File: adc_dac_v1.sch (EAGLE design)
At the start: 24 parts, among them IC2 LT6220, IC4 LT6220, U2 DAC8832IRGYR, U4 OPA353NA/3K, U7 DAC8832IRGYR, U8 OPA353NA/3K

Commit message: updates to DAC design
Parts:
- removed C16, C18: DNP, rcl:C-USC0603
- removed C17, C19, C20: 0.1u, rcl:C-USC0603
- removed IC4: LT6220, linear:MCP601SN
- removed R13, R14, R15, R16, R6, R8: 0, rcl:R-US_R0603
- removed U4, U8: OPA353NA/3K, AD7960:OPA353NA/3K
- removed U7: DAC8832IRGYR, AD7960:DAC8832IRGYR
- added C1, C2: 0.1u, rcl:C-USC0603
- added C3: 2p, rcl:C-USC0603
- added IC1: LT6220, linear:MCP601SN
- added R1: 10k, rcl:R-US_R0603
- added R2, R3: 60k, rcl:R-US_R0603
- added R4: 0, rcl:R-US_R0603
- added U1: OPA353NA/3K, open_covg:OPA353NA/3K
- U2: value DAC8832IRGYR -> AD5453YRMZ-REEL7; device AD7960:DAC8832IRGYR -> open_covg:AD5453YRMZ-REEL7
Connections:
- removed net N$15: R14.1, U7.RFB
- removed net N$16: R16.1, U7.!LDAC
- removed net N$8: R8.1, U2.!LDAC
- new net CLK+: R2.1, U1.CLK+
- new net CLK-: R2.2, U1.CLK-
- new net CNV+: U1.CNV+
- new net CNV-: U1.CNV-
- new net D+: U1.D+
- new net D-: U1.D-
- new net DCO+: U1.DCO+
- new net DCO-: U1.DCO-
- new net DIFF_IN+: R4.1
- new net EN0: U1.EN0
- new net EN1: U1.EN1
- new net EN2: U1.EN2
- new net EN3: U1.EN3
- new net IN-: U1.IN-
- new net N$1: C3.1, IC1.+IN, IC1.IN-, IC1.OUT, R1.1, U2.IOUT1
- new net N$4: IC1.OUT, R1.1, R4.2, U1.VDD2_3
- new net REF_5V: IC1.IN+
- net +5V: now also C1.1, IC1.V+, U1.VDD1, U1.VDD1_2, U1.VDD1_3; no longer C19.1, IC4.V+
- net -5V: now also C2.1, IC1.V-; no longer C20.1, IC4.V-
- net 1.8V: now also C3.1, U1.VDD2, U1.VDD2_2, U1.VIO
- net 3V3: now also C2.1, U1.V+, U1.VDD; no longer C17.1, U4.V+, U7.VDD, U8.V+
- net 3V3_REF: now also U1.IN+; no longer U4.IN+, U8.IN+
- net AGND: now also C1.2, C2.2, C3.2, IC1.-IN, IC2.-IN, R4.1, R4.2, U1.!LDAC, U1.AGNDF, U1.AGNDS, U1.DGND, U1.EPAD, U1.V-, U2.GND; no longer C16.2, C17.2, C18.2, C19.2, C20.2, R16.2, R8.2, U2.AGNDF, U2.AGNDS, U2.DGND, U2.EPAD, U4.V-, U7.AGNDF, U7.AGNDS, U7.DGND, U7.EPAD, U8.V-
- net AMP_PWR+: now also C1.1, IC1.+VS
- net CSB: now also U1.!CS, U2.SYNCB; no longer U2.!CS, U7.!CS
- net DAC_VAL: now also IC1.+IN, U1.VOUT; no longer IC2.+IN, IC4.+IN, U2.VOUT, U7.VOUT
- net GND: now also C1.2, C2.2, C3.2, IC1.-VS, R3.1, U1.EPAD, U1.GND, U1.GND_2, U1.REFIN, U1.REF_GND, U1.REF_GND_2, U1.REF_GND_3
- net IN+: now also U1.IN+; no longer R13.2
- net N$11: no longer R6.1, R8.2
- net N$12: no longer R6.2
- net N$13: no longer IC4.-IN, IC4.OUT, R14.2, R15.1, U7.INV
- net N$14: no longer R13.1, U8.OUT
- net N$2: now also C3.2, IC1.-IN, IC1.OUT, R2.2, R3.1, R4.1, R4.2, U1.INV, U2.RFB; no longer R8.1
- net N$3: now also C2.1, IC2.+IN, R1.2, R2.1, R3.2, U1.RFB
- net N$5: now also R2.2; no longer IC2.-IN, R13.1, R6.2, U2.INV
- net N$6: now also C1.1, R1.2, U1.OUT, U1.VREF-F, U1.VREF-S; no longer U4.OUT
- net N$7: now also R3.1, U2.VREF; no longer R6.1, U2.RFB
- net OUT: now also C3.1, R3.2; no longer C18.1, R15.2
- net REF: now also R1.2, U1.REF, U1.REF_2, U1.REF_3, U1.REF_4
- net SCLK: now also U1.SCLK; no longer U7.SCLK
- net SDI: now also U1.SDI, U2.SDIN; no longer U2.SDI, U7.SDI
- net VCM: now also U1.VCM
- net VREF_BUF: now also U1.IN-; no longer C16.1, R13.2, U2.VREF-F, U2.VREF-S, U4.IN-, U7.VREF-F, U7.VREF-S, U8.IN-
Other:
- note added: "VDD should match level of SPI interface VREF VR02"
- moved on the sheet: C10, C6, C7, C8, C9, IC2, R5, R7

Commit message: updates to README and tracker
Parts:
- removed U1: OPA353NA/3K, open_covg:OPA353NA/3K
- added IC3: ADA4001-2, analog-devices:ADA4692-2R
- added R6: 0, rcl:R-US_R0603
- IC2: value LT6220 -> OPA353NA3K
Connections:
- removed net CNV+: U1.CNV+
- removed net CNV-: U1.CNV-
- removed net D+: U1.D+
- removed net D-: U1.D-
- removed net DCO+: U1.DCO+
- removed net DCO-: U1.DCO-
- removed net EN0: U1.EN0
- removed net EN1: U1.EN1
- removed net EN2: U1.EN2
- removed net EN3: U1.EN3
- removed net IN+: U1.IN+
- removed net IN-: U1.IN-
- new net +15V: C9.1, IC3P.V+
- new net -15V: C10.1, IC3P.V-
- new net N$8: IC2.V+
- net +5V: no longer IC2.V+, U1.VDD1, U1.VDD1_2, U1.VDD1_3
- net -5V: no longer C10.1, IC2.V-
- net 1.8V: no longer U1.VDD2, U1.VDD2_2, U1.VIO
- net 3V3: no longer U1.V+, U1.VDD
- net 3V3_REF: now also IC2.+IN; no longer U1.IN+
- net AGND: now also IC2.V-, IC3A.IN-; no longer IC2.-IN, U1.!LDAC, U1.AGNDF, U1.AGNDS, U1.DGND, U1.EPAD, U1.V-
- net CLK+: no longer U1.CLK+
- net CLK-: no longer U1.CLK-
- net CSB: no longer U1.!CS
- net DAC_VAL: no longer U1.VOUT
- net GND: no longer U1.EPAD, U1.GND, U1.GND_2, U1.REFIN, U1.REF_GND, U1.REF_GND_2, U1.REF_GND_3
- net N$11: now also R6.1
- net N$12: now also R6.2
- net N$2: no longer U1.INV
- net N$3: now also IC3A.IN+; no longer IC2.+IN, U1.RFB
- net N$4: no longer U1.VDD2_3
- net N$5: now also IC3A.OUT; no longer IC2.OUT
- net N$6: now also IC2.OUT; no longer U1.OUT, U1.VREF-F, U1.VREF-S
- net REF: no longer U1.REF, U1.REF_2, U1.REF_3, U1.REF_4
- net SCLK: no longer U1.SCLK
- net SDI: no longer U1.SDI
- net VCM: no longer U1.VCM
- net VREF_BUF: now also IC2.-IN; no longer U1.IN-
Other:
- moved on the sheet: C6, C9, IC2, R5

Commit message: ulp cleanup
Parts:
- added BRD1: OPALKELLY_XEM6310, open_covg:OPALKELLY_XEM6310
- added C11, C12, C14, C15, C16, C17, C18: 0.1u, rcl:C-USC0805
- added C13, C5: 10u, rcl:C-USC0805
- added C19, C20: DNP, rcl:C-USC0805
- added C4: 100p, rcl:C-USC0805
- added IC4: AD8031RJ, analog-devices:AD8031RJ
- added R10, R11, R8, R9: 499, rcl:R-US_R0603
- added R12, R13: 100, rcl:R-US_R0603
- added R14, R16, R17: 0, rcl:R-US_R0603
- added R15: DNP, rcl:R-US_R0603
- added R18: DNO, rcl:R-US_R0603
- added R19, R20: 33, rcl:R-US_R0603
- added U1: AD7960BCPZ-RL7, AD7960:AD7960BCPZ-RL7
- added U3: ADA4932-1YCPZ-R7, AD7960:ADA4932-1YCPZ-R7
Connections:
- new net CNV+: R10.2, R12.2, U1.CNV+
- new net CNV-: R10.1, R12.1, U1.CNV-
- new net D+: U1.D+
- new net D-: U1.D-
- new net DCO+: U1.DCO+
- new net DCO-: U1.DCO-
- new net DGND: BRD1JP2_ODD.DGND_1
- new net EN0: U1.EN0
- new net EN1: U1.EN1
- new net EN2: U1.EN2
- new net EN3: U1.EN3
- new net IN+: C4.2, R13.2, R20.2, U1.IN+
- new net IN-: C4.1, R12.2, R19.2, U1.IN-
- new net N$10: IC4.IN-, IC4.OUT, R14.1
- new net N$15: C20.1, R10.1, R16.2, R18.1
- new net N$16: C19.1, R11.1, R15.2, R17.2
- new net N$17: R19.1, U3.OUT-
- new net N$18: R20.1, U3.OUT+
- new net N$19: BRD1JP2_ODD.JTAG_TCK
- new net N$20: BRD1JP2_ODD.JTAG_TMS
- new net N$21: BRD1JP2_ODD.JTAG_TDI
- new net N$22: BRD1JP2_ODD.G16-L9P_1
- new net N$9: U1.VDD2_3
- new net TEST_NET_NAME: BRD1JP2_EVEN.+3.3VDD_2
- net +5V: now also C11.1, C14.1, C15.1, C17.1, C4.1, U1.VDD1, U1.VDD1_2, U1.VDD1_3
- net -5V: now also C5.1
- net 1.8V: now also C11.1, C16.1, U1.VDD2, U1.VDD2_2, U1.VIO
- net 3V3: now also U1.VDD, U3.V+
- net 3V3_REF: now also U3.IN+
- net AGND: now also C4.2, C5.2, U1.!LDAC, U1.AGNDF, U1.AGNDS, U1.DGND, U1.EPAD, U3.V-
- net AMP_PWR+: now also C18.1, IC4.+VS, U3.PD, U3.VS+, U3.VS+_2, U3.VS+_3, U3.VS+_4
- net AMP_PWR-: now also U3.VS-, U3.VS-_2, U3.VS-_3, U3.VS-_4
- net CLK+: now also R13.1, U1.CLK+
- net CLK-: now also R13.2, U1.CLK-
- net CSB: now also U1.!CS
- net DAC_VAL: now also U1.VOUT
- net DIFF_IN+: now also R16.1
- net DIFF_IN-: now also R17.1
- net GND: now also C11.2, C12.2, C13.2, C14.2, C15.2, C16.2, C17.2, C18.2, C19.2, C20.2, C5.2, IC4.-VS, R11.2, R15.1, R18.2, U1.EPAD, U1.GND, U1.GND_2, U1.REFIN, U1.REF_GND, U1.REF_GND_2, U1.REF_GND_3, U3.EPAD
- net N$11: now also R10.2, R8.1, R8.2, U3.IN+
- net N$12: now also R8.2, U3.FB-
- net N$13: now also R11.2, R9.1, R9.2, U3.IN-
- net N$14: now also R9.2, U3.FB+
- net N$2: now also C12.1, R11.1, R8.1, U1.INV
- net N$3: now also R9.1, U1.RFB
- net N$4: now also U1.VDD2_3, U3.OUT
- net N$5: now also R13.1
- net N$6: now also R12.1, U1.VREF-F, U1.VREF-S, U3.IN-
- net REF: now also C12.1, C13.1, R14.2, U1.REF, U1.REF_2, U1.REF_3, U1.REF_4
- net REF_5V: now also IC4.IN+
- net SCLK: now also U1.SCLK
- net SDI: now also U1.SDI
- net VCM: now also C5.1, U1.VCM, U3.VOCM

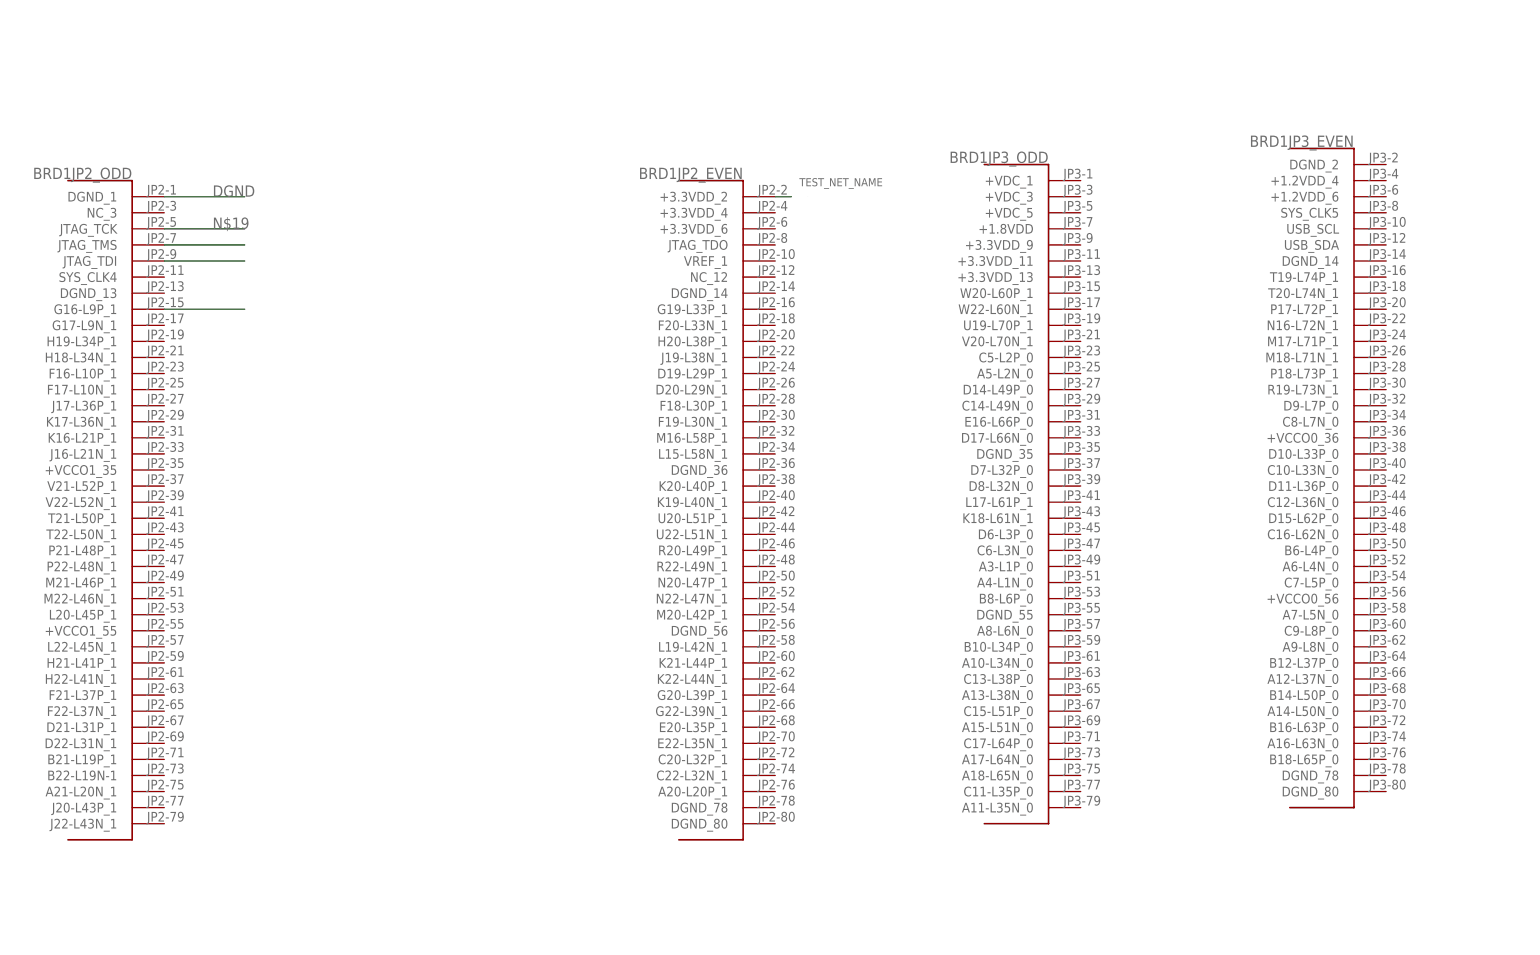
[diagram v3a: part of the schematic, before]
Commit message: updates to ULP and helper python to create script that labels samtech
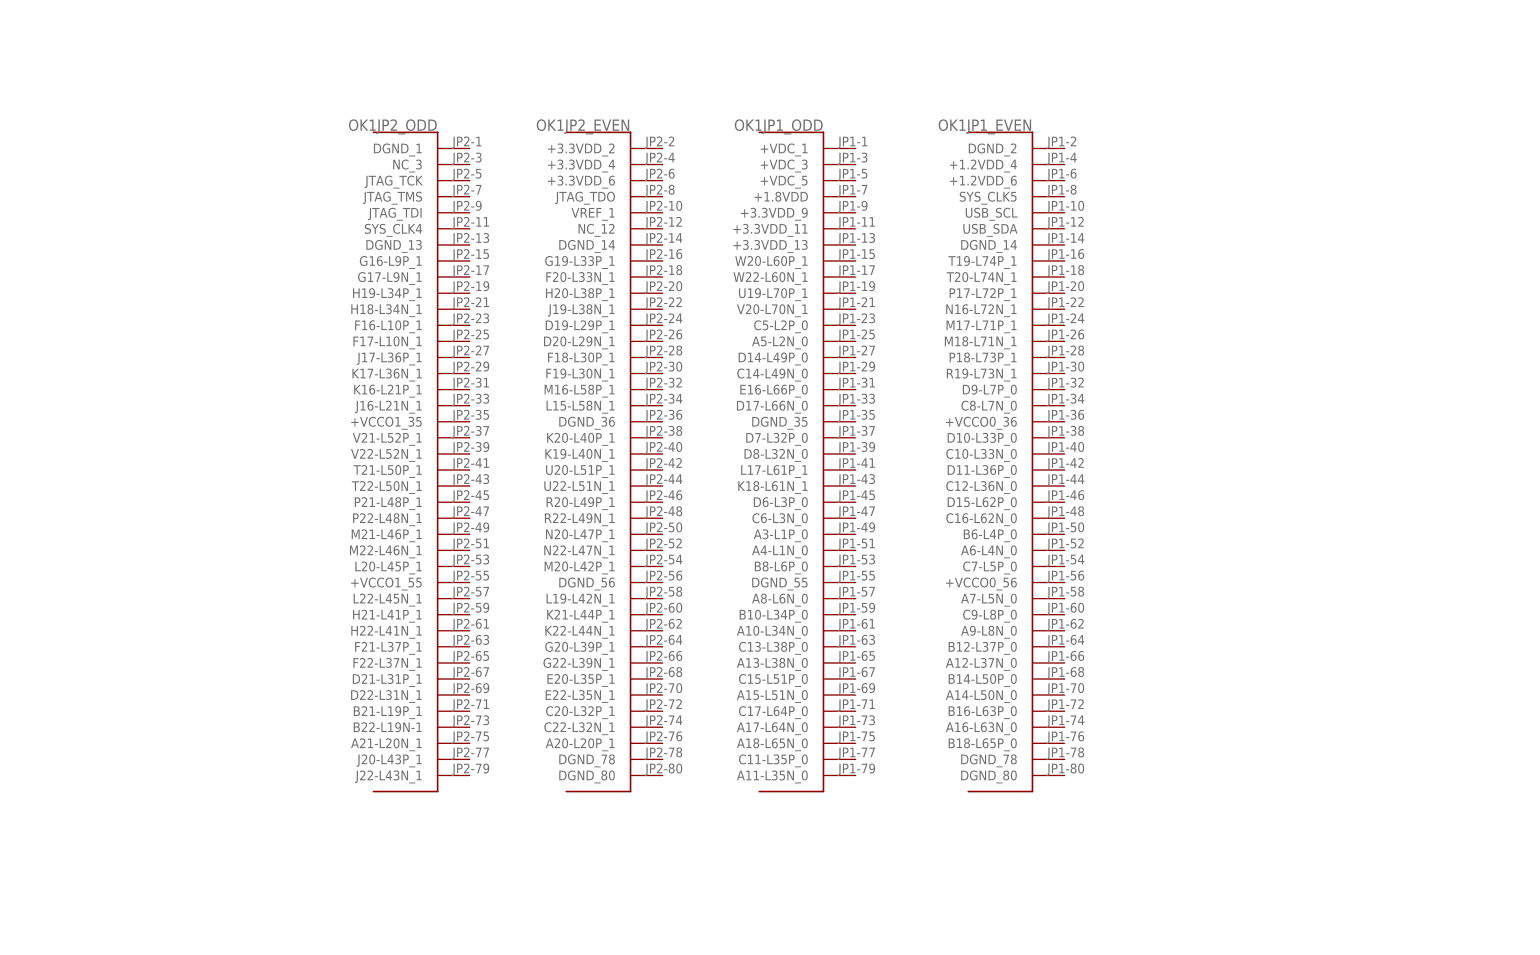
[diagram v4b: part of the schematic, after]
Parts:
- removed BRD1: OPALKELLY_XEM6310, open_covg:OPALKELLY_XEM6310
- added OK1: OPALKELLY_XEM6310, open_covg:OPALKELLY_XEM6310
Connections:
- removed net DGND: BRD1JP2_ODD.DGND_1
- removed net N$19: BRD1JP2_ODD.JTAG_TCK
- removed net N$20: BRD1JP2_ODD.JTAG_TMS
- removed net N$21: BRD1JP2_ODD.JTAG_TDI
- removed net N$22: BRD1JP2_ODD.G16-L9P_1
- removed net TEST_NET_NAME: BRD1JP2_EVEN.+3.3VDD_2
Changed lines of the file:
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@@
 <setting verticaltext="up"/>
 </settings>
-<grid distance="0.1" unitdist="inch" unit="inch" style="lines" multiple="1" display="yes" altdistance="0.01" altunitdist="inch" altunit="inch"/>
+<grid distance="0.1" unitdist="inch" unit="inch" style="lines" multiple="1" display="no" altdistance="0.01" altunitdist="inch" altunit="inch"/>
 <layers>
 <layer number="1" name="Top" color="4" fill="1" visible="no" active="no"/>
@@
 <part name="R19" library="rcl" library_urn="urn:adsk.eagle:library:334" deviceset="R-US_" device="R0603" package3d_urn="urn:adsk.eagle:package:23555/3" value="33"/>
 <part name="R20" library="rcl" library_urn="urn:adsk.eagle:library:334" deviceset="R-US_" device="R0603" package3d_urn="urn:adsk.eagle:package:23555/3" value="33"/>
-<part name="BRD1" library="open_covg" deviceset="OPALKELLY_XEM6310" device=""/>
+<part name="OK1" library="open_covg" deviceset="OPALKELLY_XEM6310" device=""/>
 </parts>
 <sheets>
@@
 <attribute name="VALUE" x="346.71" y="9.398" size="1.778" layer="96"/>
 </instance>
-<instance part="BRD1" gate="JP2_ODD" x="-27.94" y="149.86" smashed="yes">
-<attribute name="NAME" x="-22.86" y="200.914" size="1.778" layer="95" font="vector" ratio="12" rot="MR0"/>
-</instance>
-<instance part="BRD1" gate="JP2_EVEN" x="68.58" y="149.86" smashed="yes">
-<attribute name="NAME" x="73.66" y="200.914" size="1.778" layer="95" font="vector" ratio="12" rot="MR0"/>
-</instance>
-<instance part="BRD1" gate="JP3_ODD" x="116.84" y="152.4" smashed="yes">
-<attribute name="NAME" x="121.92" y="203.454" size="1.778" layer="95" font="vector" ratio="12" rot="MR0"/>
-</instance>
-<instance part="BRD1" gate="JP3_EVEN" x="165.1" y="154.94" smashed="yes">
-<attribute name="NAME" x="170.18" y="205.994" size="1.778" layer="95" font="vector" ratio="12" rot="MR0"/>
+<instance part="OK1" gate="JP2_ODD" x="20.32" y="157.48" smashed="yes">
+<attribute name="NAME" x="25.4" y="208.534" size="1.778" layer="95" font="vector" ratio="12" rot="MR0"/>
+</instance>
+<instance part="OK1" gate="JP2_EVEN" x="50.8" y="157.48" smashed="yes">
+<attribute name="NAME" x="55.88" y="208.534" size="1.778" layer="95" font="vector" ratio="12" rot="MR0"/>
+</instance>
+<instance part="OK1" gate="JP1_ODD" x="81.28" y="157.48" smashed="yes">
+<attribute name="NAME" x="86.36" y="208.534" size="1.778" layer="95" font="vector" ratio="12" rot="MR0"/>
+</instance>
+<instance part="OK1" gate="JP1_EVEN" x="114.3" y="157.48" smashed="yes">
+<attribute name="NAME" x="119.38" y="208.534" size="1.778" layer="95" font="vector" ratio="12" rot="MR0"/>
 </instance>
 </instances>
@@
 </segment>
 </net>
-<net name="DGND" class="0">
-<segment>
-<pinref part="BRD1" gate="JP2_ODD" pin="DGND_1"/>
-<wire x1="-17.78" y1="198.12" x2="-5.08" y2="198.12" width="0.1524" layer="91"/>
-<label x="-10.16" y="198.12" size="1.778" layer="95"/>
-</segment>
-</net>
-<net name="N$19" class="0">
-<segment>
-<pinref part="BRD1" gate="JP2_ODD" pin="JTAG_TCK"/>
-<wire x1="-17.78" y1="193.04" x2="-5.08" y2="193.04" width="0.1524" layer="91"/>
-<label x="-10.16" y="193.04" size="1.778" layer="95"/>
-</segment>
-</net>
-<net name="N$20" class="0">
-<segment>
-<pinref part="BRD1" gate="JP2_ODD" pin="JTAG_TMS"/>
-<wire x1="-17.78" y1="190.5" x2="-5.08" y2="190.5" width="0.1524" layer="91"/>
-</segment>
-</net>
-<net name="N$21" class="0">
-<segment>
-<pinref part="BRD1" gate="JP2_ODD" pin="JTAG_TDI"/>
-<wire x1="-17.78" y1="187.96" x2="-5.08" y2="187.96" width="0.1524" layer="91"/>
-</segment>
-</net>
-<net name="N$22" class="0">
-<segment>
-<pinref part="BRD1" gate="JP2_ODD" pin="G16-L9P_1"/>
-<wire x1="-17.78" y1="180.34" x2="-5.08" y2="180.34" width="0.1524" layer="91"/>
-</segment>
-</net>
-<net name="TEST_NET_NAME" class="0">
-<segment>
-<pinref part="BRD1" gate="JP2_EVEN" pin="+3.3VDD_2"/>
-<wire x1="78.74" y1="198.12" x2="81.28" y2="198.12" width="0.1524" layer="91"/>
-<label x="82.55" y="199.771" size="1.27" layer="95"/>
-<label x="81.28" y="198.12" size="0.010159375" layer="95"/>
-<label x="83.82" y="198.12" size="0.010159375" layer="95"/>
-<label x="83.82" y="198.12" size="0.010159375" layer="95"/>
-</segment>
-</net>
